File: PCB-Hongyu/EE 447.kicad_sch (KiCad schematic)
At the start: 9 parts, among them J1 Conn_01x04_Pin, U1 TSC2046IPWR

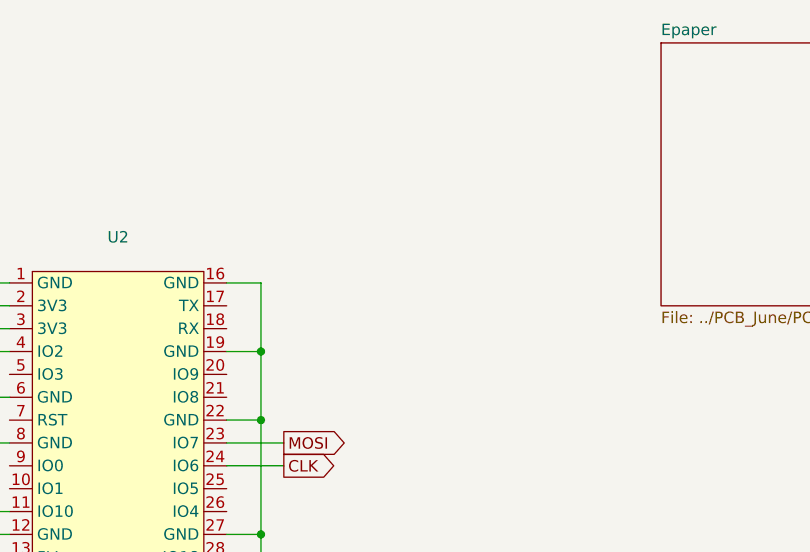
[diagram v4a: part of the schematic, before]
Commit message: routed power circuitry
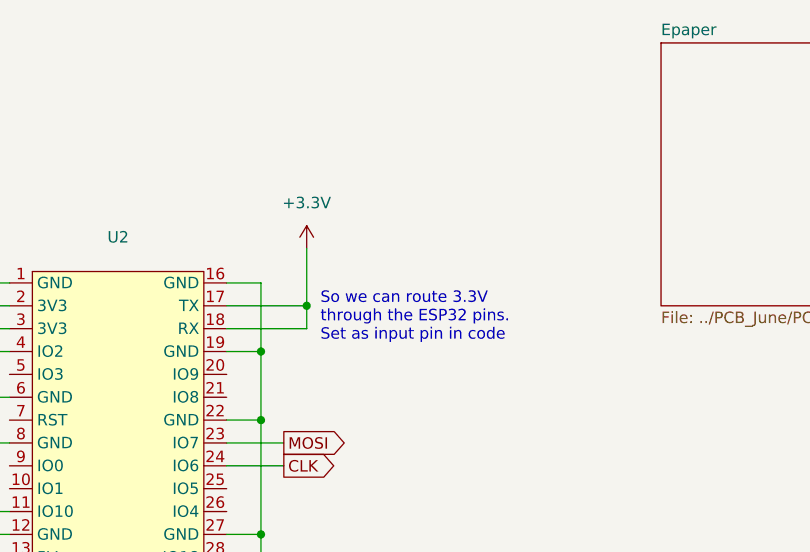
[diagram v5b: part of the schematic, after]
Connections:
- net +3.3V: now also U2.17 (TX), U2.18 (RX)
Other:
- note added: "So we can route 3.3V through the ESP32 pins. Set as input pin in code"
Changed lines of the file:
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@@
 	(generator_version "9.0")
 	(paper "A4")
+	(text "So we can route 3.3V \nthrough the ESP32 pins.\nSet as input pin in code"
+		(exclude_from_sim no)
+		(at 165.354 57.15 0)
+		(effects
+			(font
+				(size 1.27 1.27)
+			)
+			(justify left)
+		)
+	)
 	(junction
 		(at 111.76 83.82)
@@
 	(junction
 		(at 128.27 81.28)
+		(diameter 0)
+		(color 0 0 0 0)
+	)
+	(junction
+		(at 163.83 55.88)
 		(diameter 0)
 		(color 0 0 0 0)
@@
 	(wire
 		(pts
+			(xy 154.94 55.88) (xy 163.83 55.88)
+		)
+		(stroke
+			(width 0)
+			(type default)
+		)
+	)
+	(wire
+		(pts
 			(xy 90.17 113.03) (xy 90.17 119.38)
 		)
@@
 	(wire
 		(pts
+			(xy 154.94 58.42) (xy 163.83 58.42)
+		)
+		(stroke
+			(width 0)
+			(type default)
+		)
+	)
+	(wire
+		(pts
 			(xy 93.98 86.36) (xy 106.68 86.36)
 		)
@@
 	(wire
 		(pts
+			(xy 163.83 58.42) (xy 163.83 55.88)
+		)
+		(stroke
+			(width 0)
+			(type default)
+		)
+	)
+	(wire
+		(pts
 			(xy 52.07 105.41) (xy 52.07 119.38)
 		)
@@
 		(pts
 			(xy 106.68 102.87) (xy 106.68 86.36)
+		)
+		(stroke
+			(width 0)
+			(type default)
+		)
+	)
+	(wire
+		(pts
+			(xy 163.83 49.53) (xy 163.83 55.88)
 		)
 		(stroke
@@
 			)
 		)
+	)
+	(symbol
+		(lib_id "power:+3.3V")
+		(at 163.83 49.53 0)
+		(unit 1)
+		(exclude_from_sim no)
+		(in_bom yes)
+		(on_board yes)
+		(dnp no)
+		(fields_autoplaced yes)
+		(property "Reference" "#PWR019"
+			(at 163.83 53.34 0)
+			(effects
+				(font
+					(size 1.27 1.27)
+				)
+				(hide yes)
+			)
+		)
+		(property "Value" "+3.3V"
+			(at 163.83 44.45 0)
+			(effects
+				(font
+					(size 1.27 1.27)
+				)
+			)
+		)
+		(property "Footprint" ""
+			(at 163.83 49.53 0)
+			(effects
+				(font
+					(size 1.27 1.27)
+				)
+				(hide yes)
+			)
+		)
+		(property "Datasheet" ""
+			(at 163.83 49.53 0)
+			(effects
+				(font
+					(size 1.27 1.27)
+				)
+				(hide yes)
+			)
+		)
+		(property "Description" "Power symbol creates a global label with name \"+3.3V\""
+			(at 163.83 49.53 0)
+			(effects
+				(font
+					(size 1.27 1.27)
+				)
+				(hide yes)
+			)
+		)
+		(pin "1"
+		)
+		(instances
+			(project "EE 447"
+				(path "/8dcae476-bf02-4dea-8567-670805b7ab7c"
+					(reference "#PWR019")
+					(unit 1)
+				)
+			)
+		)

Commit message: touch ic mostly routed
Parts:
- C6: footprint Capacitor_SMD:C_0805_2012Metric -> Capacitor_SMD:C_0805_2012Metric_Pad1.18x1.45mm_HandSolder
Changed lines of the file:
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@@
 			)
 		)
-		(property "Footprint" "Capacitor_SMD:C_0805_2012Metric"
+		(property "Footprint" "Capacitor_SMD:C_0805_2012Metric_Pad1.18x1.45mm_HandSolder"
 			(at 94.9452 95.25 0)
 			(effects

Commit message: hhhhh
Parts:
- U1: footprint Library:PW16 -> PW16
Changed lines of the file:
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@@
 			)
 		)
-		(property "Description" ""
+		(property "Description" "Power symbol creates a global label with name \"+BATT\""
 			(at 111.76 74.93 0)
 			(effects
@@
 			)
 		)
-		(property "Footprint" "Library:PW16"
+		(property "Footprint" "PW16"
 			(at 110.49 102.87 0)
 			(effects
